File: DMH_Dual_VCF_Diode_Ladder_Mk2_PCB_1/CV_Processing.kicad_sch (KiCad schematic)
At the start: 48 parts, among them J15 Conn_01x08_PinHeader, J16 Conn_01x08_PinHeader, SW10 SW_DPDT_OnOn, SW7 SW_SPDT_OnOffOn, SW9 SW_SPDT_OnOffOn, U7 TL074, U8 TL074

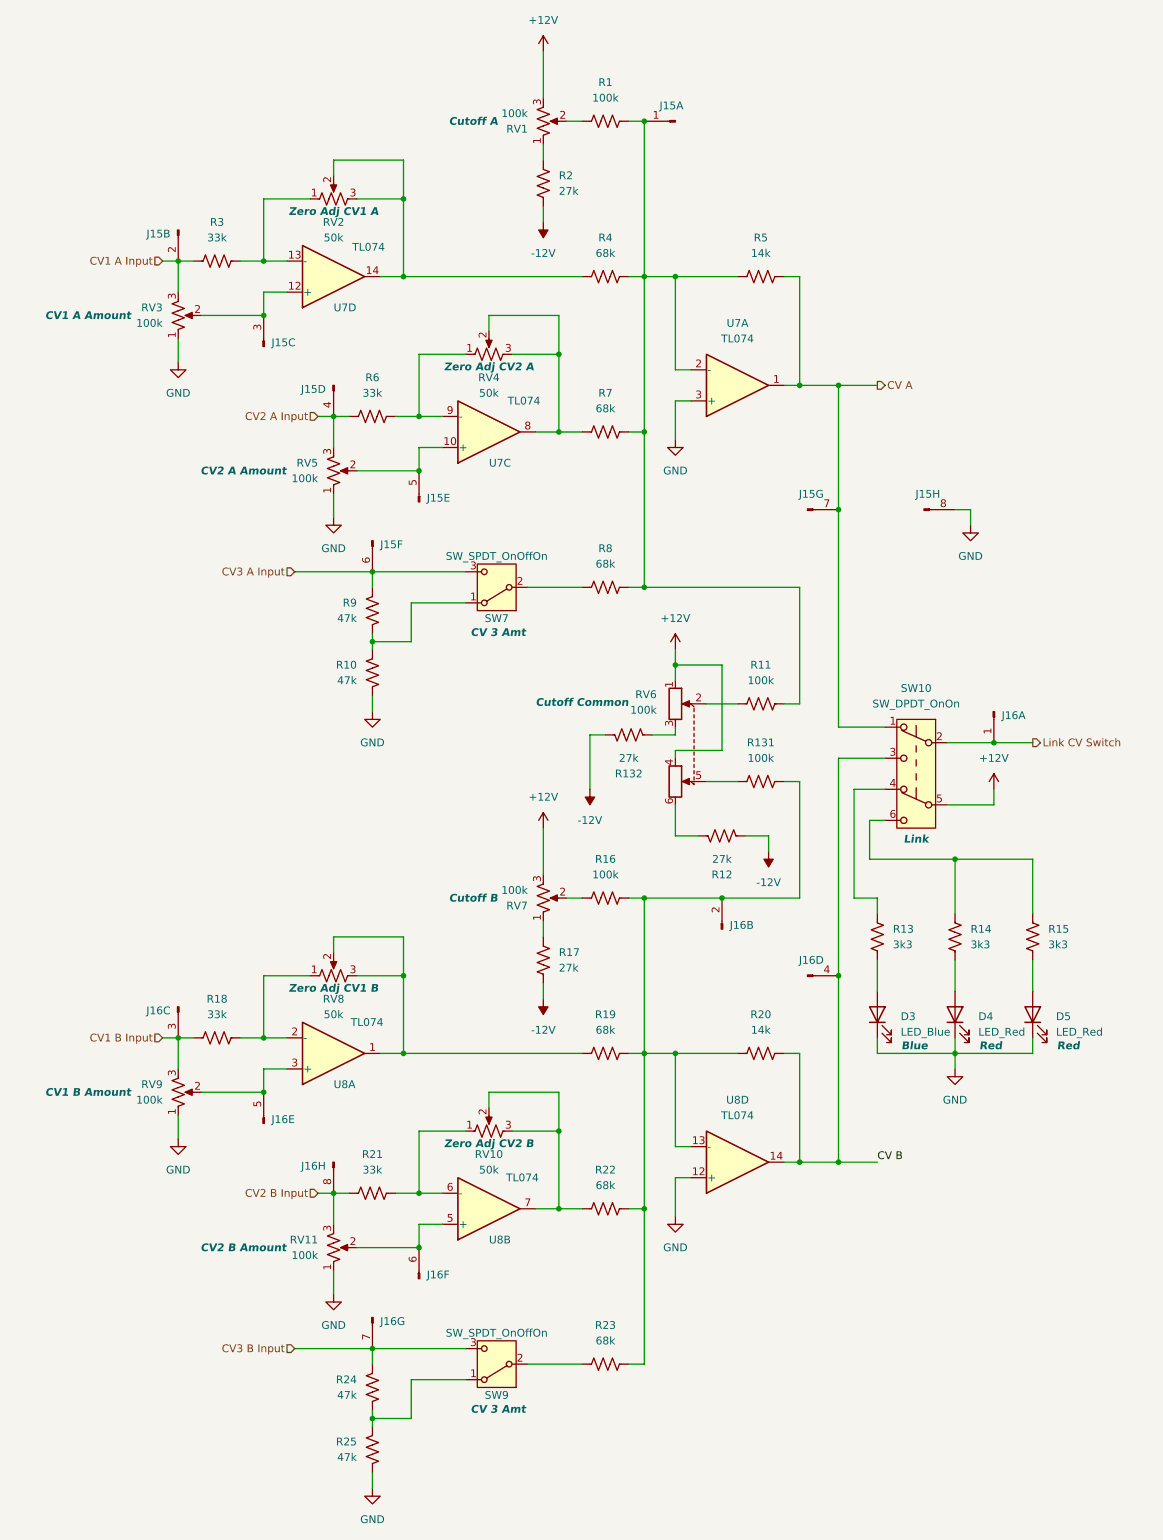
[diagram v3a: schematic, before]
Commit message: Adjusted pin header connections
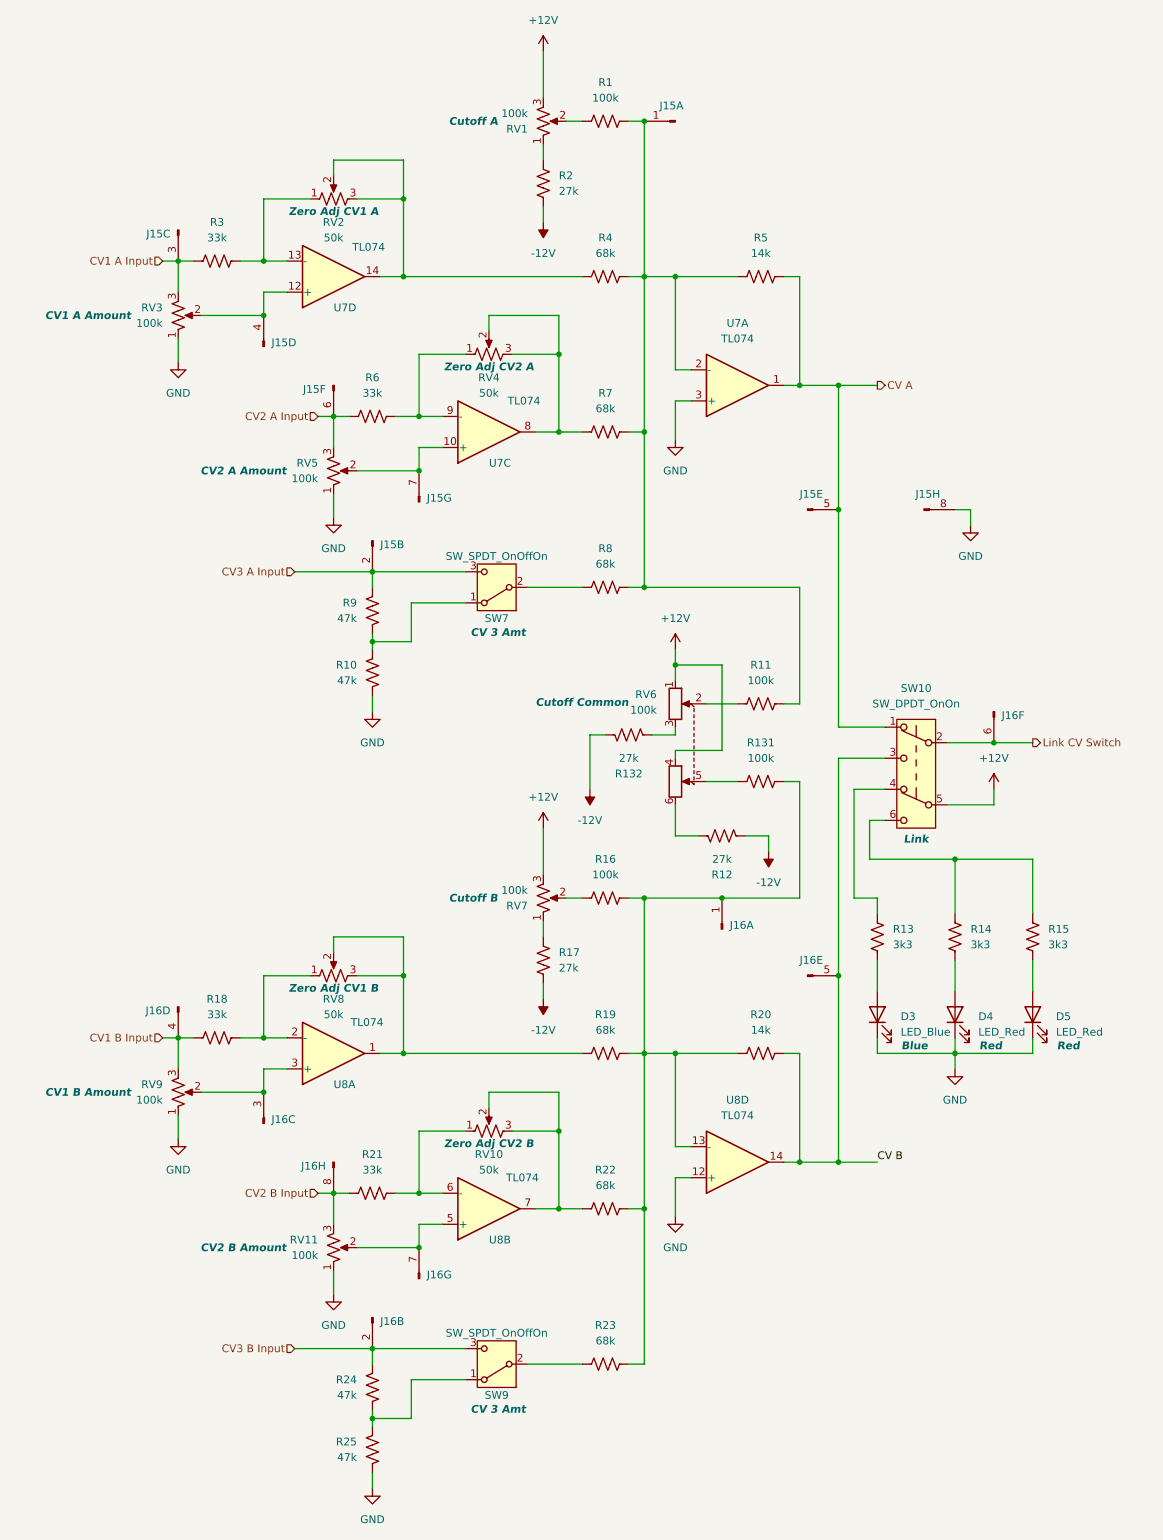
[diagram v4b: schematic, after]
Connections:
- net CV A: now also J15.5 (Pin_5); no longer J15.7 (Pin_7)
- net CV B: now also J16.5 (Pin_5); no longer J16.4 (Pin_4)
- net CV1 A Input: now also J15.3 (Pin_3); no longer J15.2 (Pin_2)
- net CV1 B Input: now also J16.4 (Pin_4); no longer J16.3 (Pin_3)
- net CV2 A Input: now also J15.6 (Pin_6); no longer J15.4 (Pin_4)
- net CV3 A Input: now also J15.2 (Pin_2); no longer J15.6 (Pin_6)
- net CV3 B Input: now also J16.2 (Pin_2); no longer J16.7 (Pin_7)
- net Link CV Switch: now also J16.6 (Pin_6); no longer J16.1 (Pin_1)
- net at R131.2, R16.2, R19.2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: now also J16.1 (Pin_1); no longer J16.2 (Pin_2)
- net at RV11.2, U8.5 (+): now also J16.7 (Pin_7); no longer J16.6 (Pin_6)
- net at RV9.2, U8.3 (+): now also J16.3 (Pin_3); no longer J16.5 (Pin_5)
- net at RV3.2, U7.12 (+): now also J15.4 (Pin_4); no longer J15.3 (Pin_3)
- net at RV5.2, U7.10 (+): now also J15.7 (Pin_7); no longer J15.5 (Pin_5)
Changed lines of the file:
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@@
 		(lib_id "SynthStuff:Conn_01x08_PinHeader")
 		(at 69.85 106.68 270)
-		(unit 6)
+		(unit 2)
 		(exclude_from_sim no)
 		(in_bom yes)
@@
 				(path "/58f4306d-5387-4983-bb08-41a2313fd315/ec2d44bc-ed06-4f0b-a22e-df640fa5e089"
 					(reference "J15")
-					(unit 6)
+					(unit 2)
 				)
 			)
@@
 		(lib_id "SynthStuff:Conn_01x08_PinHeader")
 		(at 63.5 81.28 270)
-		(unit 4)
+		(unit 6)
 		(exclude_from_sim no)
 		(in_bom yes)
@@
 				(path "/58f4306d-5387-4983-bb08-41a2313fd315/ec2d44bc-ed06-4f0b-a22e-df640fa5e089"
 					(reference "J15")
-					(unit 4)
+					(unit 6)
 				)
 			)
@@
 		(lib_id "SynthStuff:Conn_01x08_PinHeader")
 		(at 140.97 101.6 0)
-		(unit 7)
+		(unit 5)
 		(exclude_from_sim no)
 		(in_bom yes)
@@
 				(path "/58f4306d-5387-4983-bb08-41a2313fd315/ec2d44bc-ed06-4f0b-a22e-df640fa5e089"
 					(reference "J15")
-					(unit 7)
+					(unit 5)
 				)
 			)
@@
 		(at 52.07 201.93 270)
 		(mirror x)
-		(unit 5)
+		(unit 3)
 		(exclude_from_sim no)
 		(in_bom yes)
@@
 				(path "/58f4306d-5387-4983-bb08-41a2313fd315/ec2d44bc-ed06-4f0b-a22e-df640fa5e089"
 					(reference "J16")
-					(unit 5)
+					(unit 3)
 				)
 			)
@@
 		(lib_id "SynthStuff:Conn_01x08_PinHeader")
 		(at 127 170.18 90)
-		(unit 2)
+		(unit 1)
 		(exclude_from_sim no)
 		(in_bom yes)
@@
 				(path "/58f4306d-5387-4983-bb08-41a2313fd315/ec2d44bc-ed06-4f0b-a22e-df640fa5e089"
 					(reference "J16")
-					(unit 2)
+					(unit 1)
 				)
 			)
@@
 		(at 38.1 182.88 90)
 		(mirror x)
-		(unit 3)
+		(unit 4)
 		(exclude_from_sim no)
 		(in_bom yes)
@@
 				(path "/58f4306d-5387-4983-bb08-41a2313fd315/ec2d44bc-ed06-4f0b-a22e-df640fa5e089"
 					(reference "J16")
-					(unit 3)
+					(unit 4)
 				)
 			)
@@
 		(lib_id "SynthStuff:Conn_01x08_PinHeader")
 		(at 77.47 227.33 90)
-		(unit 6)
+		(unit 7)
 		(exclude_from_sim no)
 		(in_bom yes)
@@
 				(path "/58f4306d-5387-4983-bb08-41a2313fd315/ec2d44bc-ed06-4f0b-a22e-df640fa5e089"
 					(reference "J16")
-					(unit 6)
+					(unit 7)
 				)
 			)
@@
 		(at 77.47 100.33 270)
 		(mirror x)
-		(unit 5)
+		(unit 7)
 		(exclude_from_sim no)
 		(in_bom yes)
@@
 				(path "/58f4306d-5387-4983-bb08-41a2313fd315/ec2d44bc-ed06-4f0b-a22e-df640fa5e089"
 					(reference "J15")
-					(unit 5)
+					(unit 7)
 				)
 			)
@@
 		(lib_id "SynthStuff:Conn_01x08_PinHeader")
 		(at 140.97 177.8 0)
-		(unit 4)
+		(unit 5)
 		(exclude_from_sim no)
 		(in_bom yes)
@@
 				(path "/58f4306d-5387-4983-bb08-41a2313fd315/ec2d44bc-ed06-4f0b-a22e-df640fa5e089"
 					(reference "J16")
-					(unit 4)
+					(unit 5)
 				)
 			)
@@
 		(lib_id "SynthStuff:Conn_01x08_PinHeader")
 		(at 171.45 134.62 270)
-		(unit 1)
+		(unit 6)
 		(exclude_from_sim no)
 		(in_bom yes)
@@
 				(path "/58f4306d-5387-4983-bb08-41a2313fd315/ec2d44bc-ed06-4f0b-a22e-df640fa5e089"
 					(reference "J16")
-					(unit 1)
+					(unit 6)
 				)
 			)
@@
 		(at 38.1 55.88 90)
 		(mirror x)
-		(unit 2)
+		(unit 3)
 		(exclude_from_sim no)
 		(in_bom yes)
@@
 				(path "/58f4306d-5387-4983-bb08-41a2313fd315/ec2d44bc-ed06-4f0b-a22e-df640fa5e089"
 					(reference "J15")
-					(unit 2)
+					(unit 3)
 				)
 			)
@@
 		(lib_id "SynthStuff:Conn_01x08_PinHeader")
 		(at 52.07 74.93 90)
-		(unit 3)
+		(unit 4)
 		(exclude_from_sim no)
 		(in_bom yes)
@@
 				(path "/58f4306d-5387-4983-bb08-41a2313fd315/ec2d44bc-ed06-4f0b-a22e-df640fa5e089"
 					(reference "J15")
-					(unit 3)
+					(unit 4)
 				)
 			)
@@
 		(lib_id "SynthStuff:Conn_01x08_PinHeader")
 		(at 69.85 233.68 270)
-		(unit 7)
+		(unit 2)
 		(exclude_from_sim no)
 		(in_bom yes)
@@
 				(path "/58f4306d-5387-4983-bb08-41a2313fd315/ec2d44bc-ed06-4f0b-a22e-df640fa5e089"
 					(reference "J16")
-					(unit 7)
+					(unit 2)
 				)
 			)

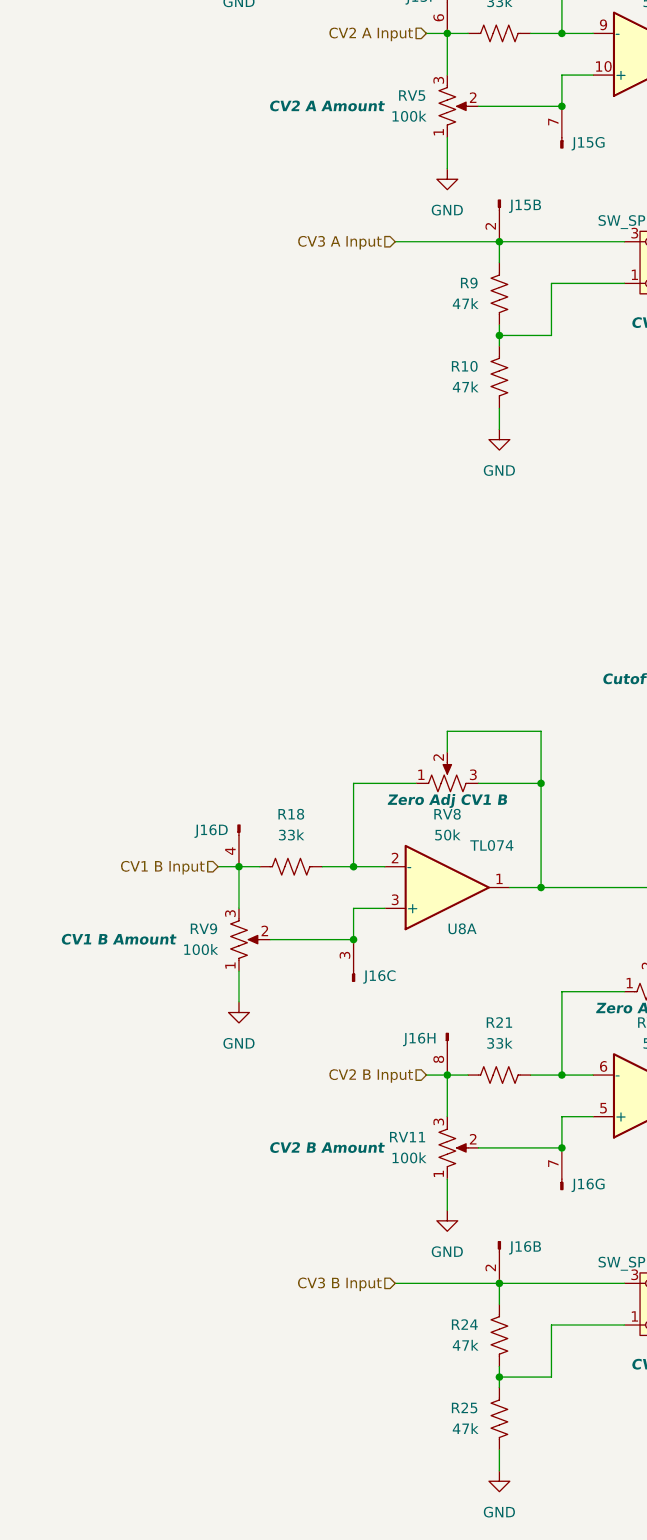
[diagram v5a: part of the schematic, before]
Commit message: Adding buffered input to CV3 - in progress
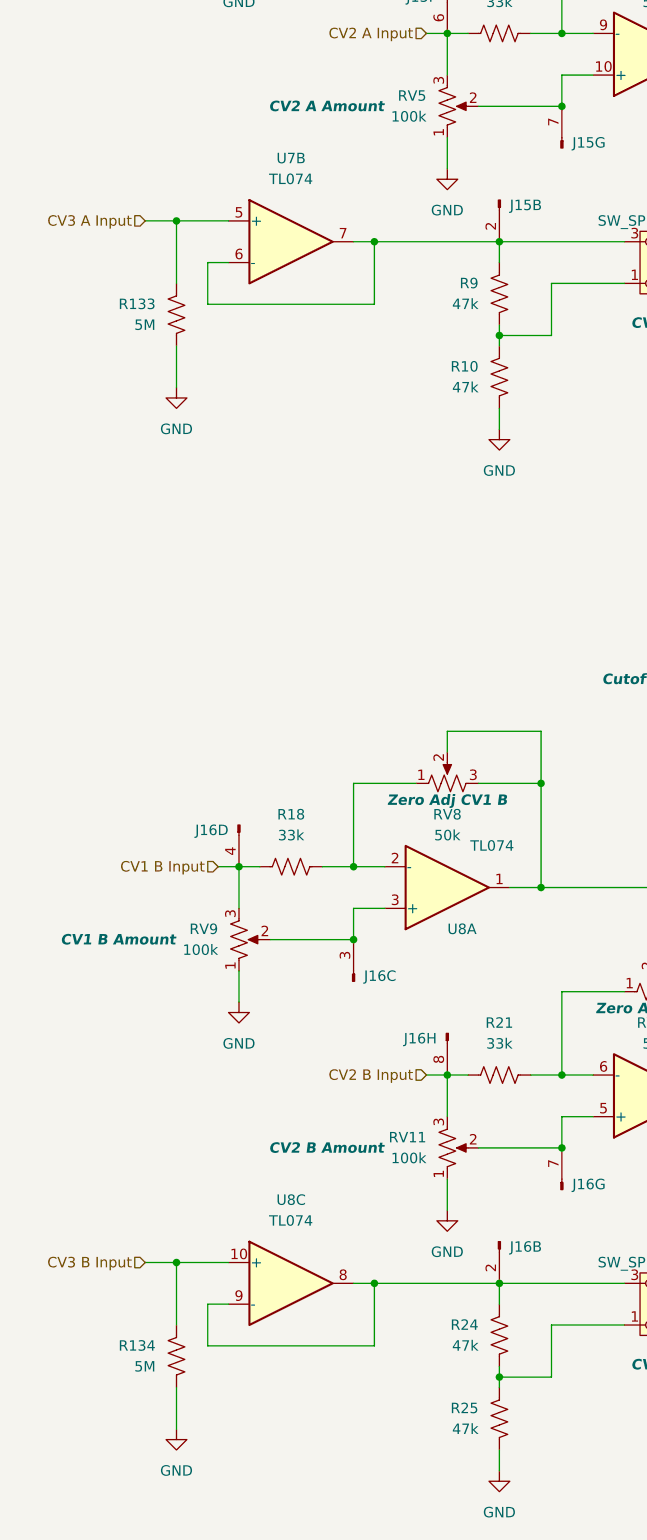
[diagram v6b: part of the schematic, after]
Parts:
- added R133, R134: 5M, Resistor_THT:R_Axial_DIN0207_L6.3mm_D2.5mm_P7.62mm_Horizontal, symbol Device:R_US
- added unit 2 of U7
- added unit 3 of U8
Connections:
- net CV3 A Input: now also R133.2, U7.5 (+); no longer J15.2 (Pin_2), R9.2, SW7.3 (C)
- net CV3 B Input: now also R134.2, U8.10 (+); no longer J16.2 (Pin_2), R24.2, SW9.3 (C)
- net GND: now also R133.1, R134.1
- new net: J15.2 (Pin_2), R9.2, SW7.3 (C), U7.6 (-), U7.7
- new net: J16.2 (Pin_2), R24.2, SW9.3 (C), U8.8, U8.9 (-)

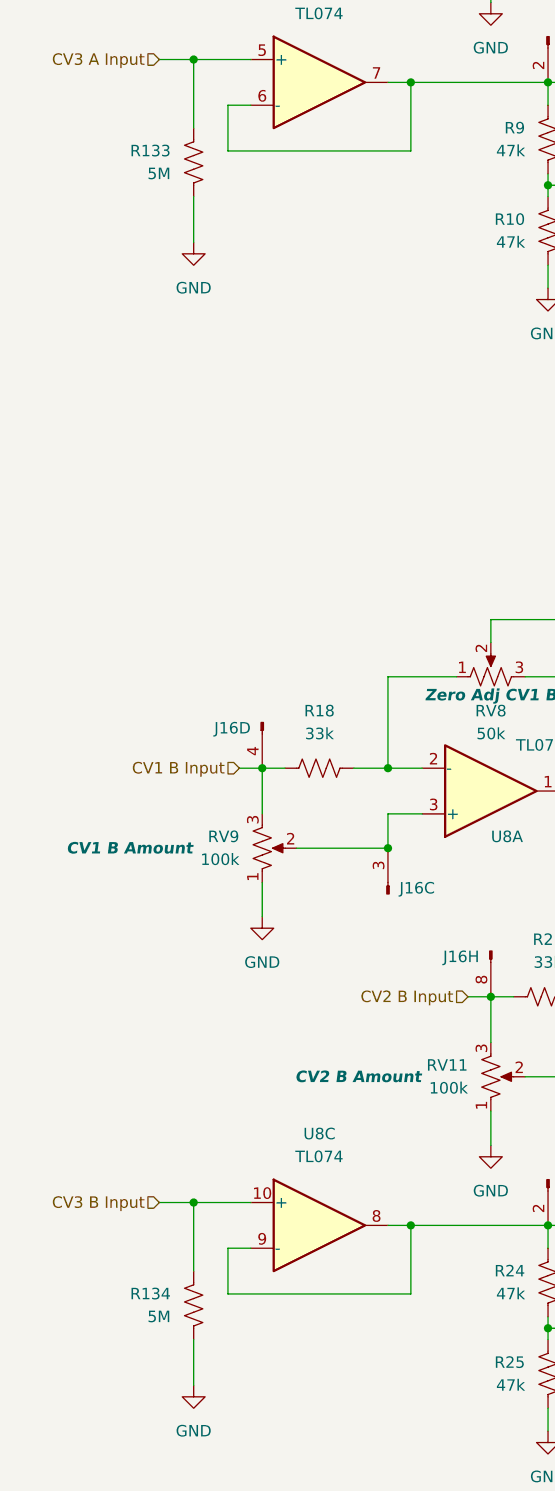
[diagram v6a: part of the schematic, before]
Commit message: Added buffering to each CV 3 input separately
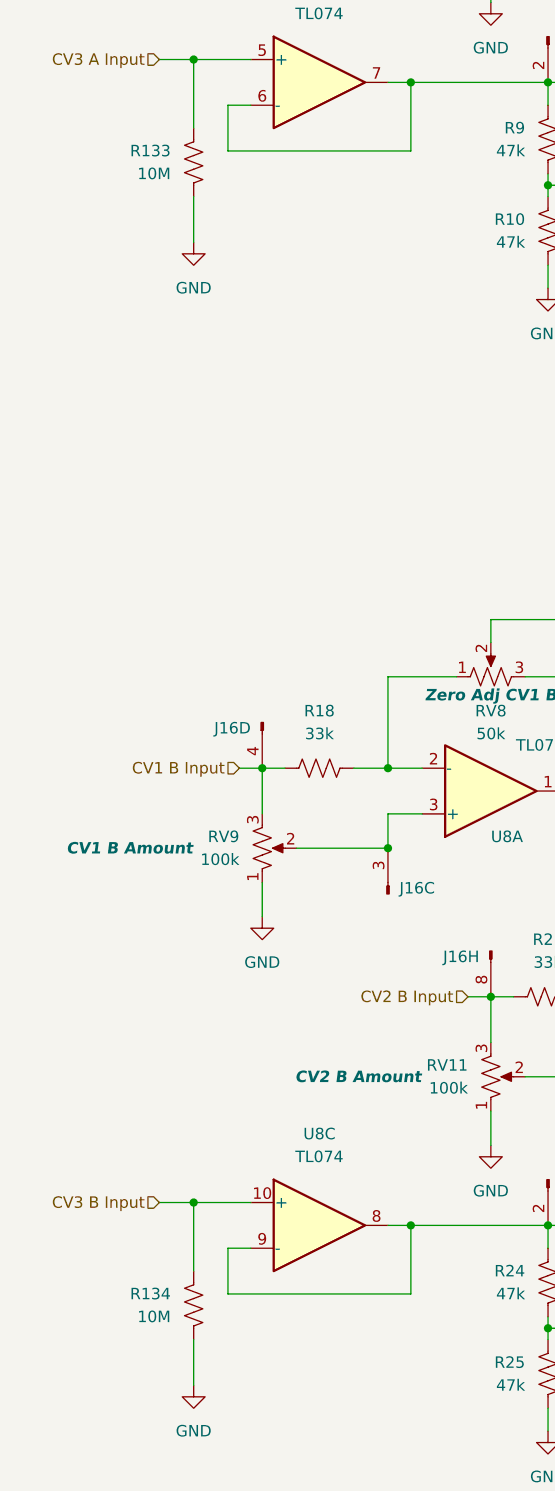
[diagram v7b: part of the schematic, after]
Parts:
- R133, R134: value 5M -> 10M
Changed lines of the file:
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@@
 			)
 		)
-		(property "Value" "5M"
+		(property "Value" "10M"
 			(at 27.94 248.9199 0)
 			(effects
@@
 			)
 		)
-		(property "Value" "5M"
+		(property "Value" "10M"
 			(at 27.94 121.9199 0)
 			(effects
